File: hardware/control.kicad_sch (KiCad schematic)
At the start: 11 parts, among them J7 ESP32_DISP_P1, J8 ESP32_DISP_CN1, U1 MCP23017-E/SO, U2 TMP275AIDR

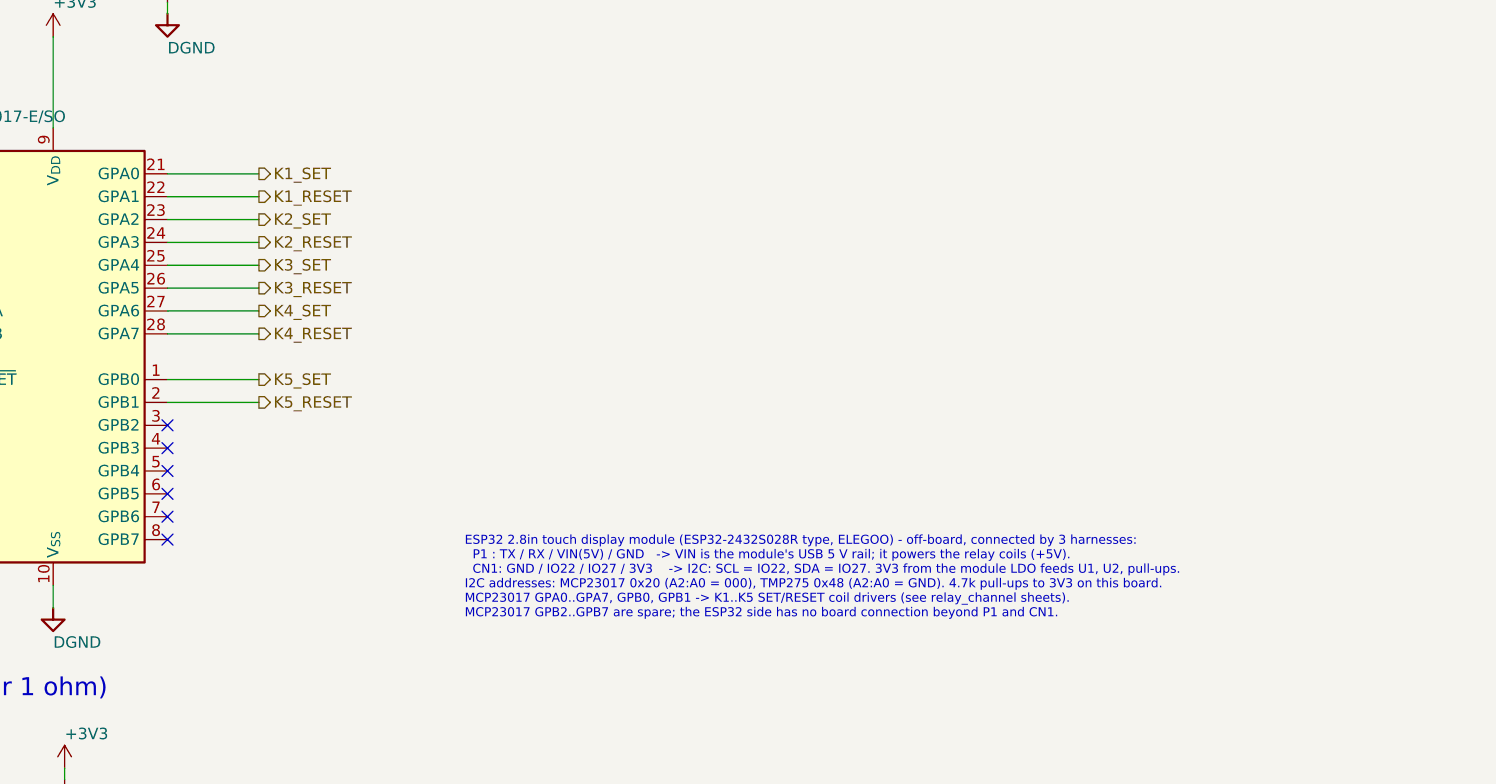
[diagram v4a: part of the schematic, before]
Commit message: Remap the MCP23017 GPIOs to the driver order: fan-out 30 vias -> 0
The coil lines were on GPA0..GPA7 (+ GPB0/1 for K5): the package row that
faces the board edge, in an order scrambled against the driver columns,
while GPB2..GPB7 - the row facing the drivers - sat unused. Every line had
to get off the wrong side of the chip and cross its neighbours.

  GPB0..GPB7  K4 S, K4 R, K1 S, K1 R, K2 S, K2 R, K3 S, K3 R  (columns' order)
  GPA0/GPA1   K5 RESET / K5 SET  (leave under the package to the right)
  GPA2..GPA7  spare

The firmware maps GPIO to coil by table; there is no firmware yet, so the
remap costs nothing there. Schematic change is in gen_schematics.py; only
control.kicad_sch changes, ERC clean, board nets synced from the netlist.

The whole control band is now hand-laid in route_hand.py: the fan-out, SDA/
SCL/3V3 under U1's body in pin order, ~RESET along the top edge, the harness
feeds between C3 and C4, +5V down the left edge, and straight B.Cu risers
from the TMP275 spine to the bus.

  MCP23017 coil lines   237 mm, 30 vias  ->  161 mm, 0 vias
  vias, whole board     101              ->  68

Also:
  route_pcb.py  vias now keep SEP from the other precision class. Two SRC_P
                vias sat 0.46 mm from RANGE_BUS; now 0 pairs under 0.5 mm.
  pcb_io.py     apply failed silently (never saved) on a board that already
                had tracks: GetNetsByName() breaks once tracks are removed.
                Look nets up with FindNet, and fail loudly if one is missing.

DRC: 0 errors, 0 unconnected, 0 schematic-parity issues, 56 benign
silk_over_copper. Silkscreen from the hand pass is untouched.

Co-Authored-By: Claude Opus 5 <noreply@anthropic.com>
Claude-Session: https://claude.ai/code/session_0128rWrsZDfCzkxQ1CZFxeXp
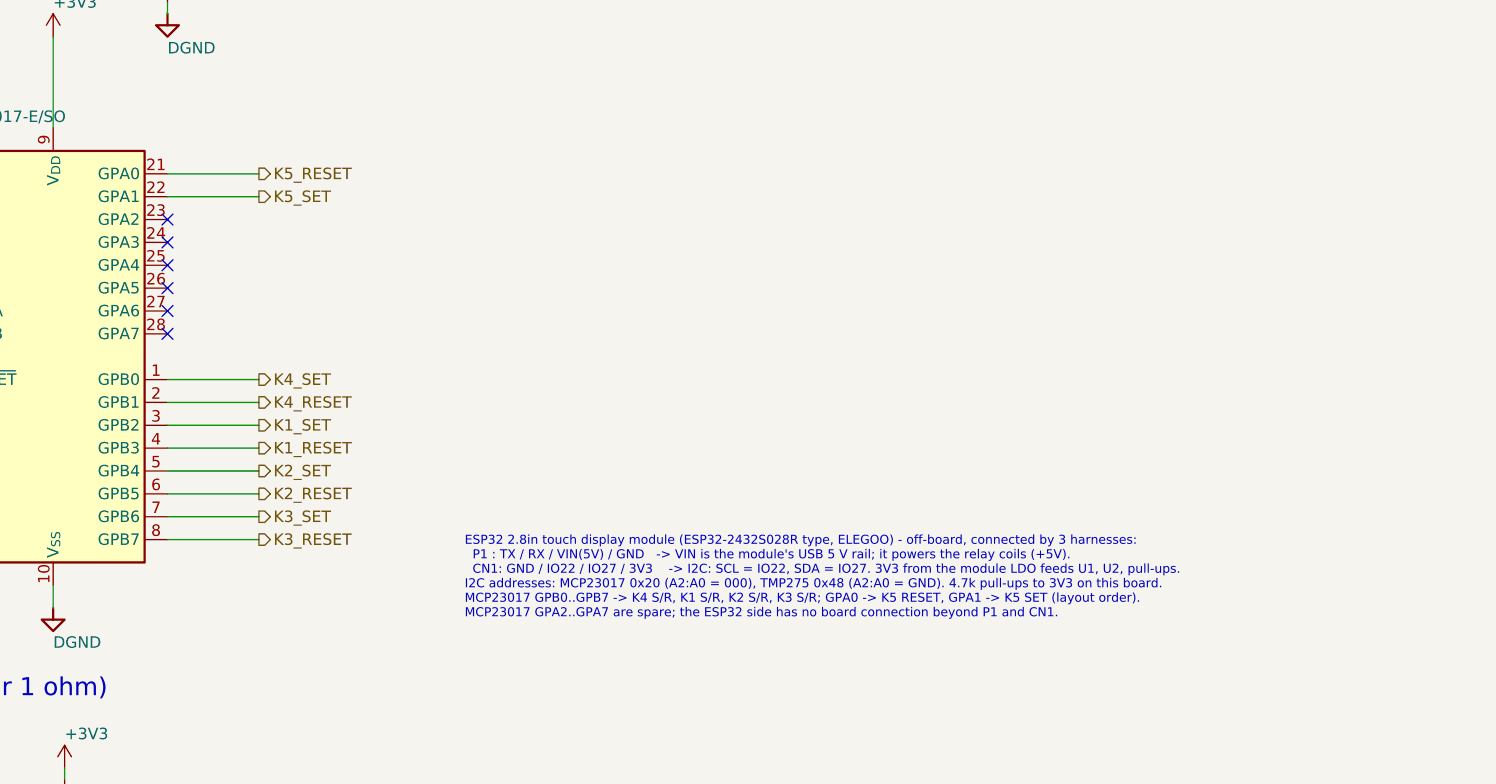
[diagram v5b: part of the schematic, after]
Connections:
- net K1_RESET: now also U1.4 (GPB3); no longer U1.22 (GPA1)
- net K1_SET: now also U1.3 (GPB2); no longer U1.21 (GPA0)
- net K2_RESET: now also U1.6 (GPB5); no longer U1.24 (GPA3)
- net K2_SET: now also U1.5 (GPB4); no longer U1.23 (GPA2)
- net K3_RESET: now also U1.8 (GPB7); no longer U1.26 (GPA5)
- net K3_SET: now also U1.7 (GPB6); no longer U1.25 (GPA4)
- net K4_RESET: now also U1.2 (GPB1); no longer U1.28 (GPA7)
- net K4_SET: now also U1.1 (GPB0); no longer U1.27 (GPA6)
- net K5_RESET: now also U1.21 (GPA0); no longer U1.2 (GPB1)
- net K5_SET: now also U1.22 (GPA1); no longer U1.1 (GPB0)
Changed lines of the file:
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@@
 	  ))
 	)
+	(wire (pts (xy 139.7 116.84) (xy 149.86 116.84)) (stroke (width 0) (type default)))
+	(hierarchical_label "K4_SET" (shape output) (at 149.86 116.84 0) (effects (font (size 1.27 1.27)) (justify left)))
+	(wire (pts (xy 139.7 119.38) (xy 149.86 119.38)) (stroke (width 0) (type default)))
+	(hierarchical_label "K4_RESET" (shape output) (at 149.86 119.38 0) (effects (font (size 1.27 1.27)) (justify left)))
+	(wire (pts (xy 139.7 121.92) (xy 149.86 121.92)) (stroke (width 0) (type default)))
+	(hierarchical_label "K1_SET" (shape output) (at 149.86 121.92 0) (effects (font (size 1.27 1.27)) (justify left)))
+	(wire (pts (xy 139.7 124.46) (xy 149.86 124.46)) (stroke (width 0) (type default)))
+	(hierarchical_label "K1_RESET" (shape output) (at 149.86 124.46 0) (effects (font (size 1.27 1.27)) (justify left)))
+	(wire (pts (xy 139.7 127) (xy 149.86 127)) (stroke (width 0) (type default)))
+	(hierarchical_label "K2_SET" (shape output) (at 149.86 127 0) (effects (font (size 1.27 1.27)) (justify left)))
+	(wire (pts (xy 139.7 129.54) (xy 149.86 129.54)) (stroke (width 0) (type default)))
+	(hierarchical_label "K2_RESET" (shape output) (at 149.86 129.54 0) (effects (font (size 1.27 1.27)) (justify left)))
+	(wire (pts (xy 139.7 132.08) (xy 149.86 132.08)) (stroke (width 0) (type default)))
+	(hierarchical_label "K3_SET" (shape output) (at 149.86 132.08 0) (effects (font (size 1.27 1.27)) (justify left)))
+	(wire (pts (xy 139.7 134.62) (xy 149.86 134.62)) (stroke (width 0) (type default)))
+	(hierarchical_label "K3_RESET" (shape output) (at 149.86 134.62 0) (effects (font (size 1.27 1.27)) (justify left)))
 	(wire (pts (xy 139.7 93.98) (xy 149.86 93.98)) (stroke (width 0) (type default)))
-	(hierarchical_label "K1_SET" (shape output) (at 149.86 93.98 0) (effects (font (size 1.27 1.27)) (justify left)))
+	(hierarchical_label "K5_RESET" (shape output) (at 149.86 93.98 0) (effects (font (size 1.27 1.27)) (justify left)))
 	(wire (pts (xy 139.7 96.52) (xy 149.86 96.52)) (stroke (width 0) (type default)))
-	(hierarchical_label "K1_RESET" (shape output) (at 149.86 96.52 0) (effects (font (size 1.27 1.27)) (justify left)))
-	(wire (pts (xy 139.7 99.06) (xy 149.86 99.06)) (stroke (width 0) (type default)))
-	(hierarchical_label "K2_SET" (shape output) (at 149.86 99.06 0) (effects (font (size 1.27 1.27)) (justify left)))
-	(wire (pts (xy 139.7 101.6) (xy 149.86 101.6)) (stroke (width 0) (type default)))
-	(hierarchical_label "K2_RESET" (shape output) (at 149.86 101.6 0) (effects (font (size 1.27 1.27)) (justify left)))
-	(wire (pts (xy 139.7 104.14) (xy 149.86 104.14)) (stroke (width 0) (type default)))
-	(hierarchical_label "K3_SET" (shape output) (at 149.86 104.14 0) (effects (font (size 1.27 1.27)) (justify left)))
-	(wire (pts (xy 139.7 106.68) (xy 149.86 106.68)) (stroke (width 0) (type default)))
-	(hierarchical_label "K3_RESET" (shape output) (at 149.86 106.68 0) (effects (font (size 1.27 1.27)) (justify left)))
-	(wire (pts (xy 139.7 109.22) (xy 149.86 109.22)) (stroke (width 0) (type default)))
-	(hierarchical_label "K4_SET" (shape output) (at 149.86 109.22 0) (effects (font (size 1.27 1.27)) (justify left)))
-	(wire (pts (xy 139.7 111.76) (xy 149.86 111.76)) (stroke (width 0) (type default)))
-	(hierarchical_label "K4_RESET" (shape output) (at 149.86 111.76 0) (effects (font (size 1.27 1.27)) (justify left)))
-	(wire (pts (xy 139.7 116.84) (xy 149.86 116.84)) (stroke (width 0) (type default)))
-	(hierarchical_label "K5_SET" (shape output) (at 149.86 116.84 0) (effects (font (size 1.27 1.27)) (justify left)))
-	(wire (pts (xy 139.7 119.38) (xy 149.86 119.38)) (stroke (width 0) (type default)))
-	(hierarchical_label "K5_RESET" (shape output) (at 149.86 119.38 0) (effects (font (size 1.27 1.27)) (justify left)))
-	(no_connect (at 139.7 121.92))
-	(no_connect (at 139.7 124.46))
-	(no_connect (at 139.7 127))
-	(no_connect (at 139.7 129.54))
-	(no_connect (at 139.7 132.08))
-	(no_connect (at 139.7 134.62))
+	(hierarchical_label "K5_SET" (shape output) (at 149.86 96.52 0) (effects (font (size 1.27 1.27)) (justify left)))
+	(no_connect (at 139.7 99.06))
+	(no_connect (at 139.7 101.6))
+	(no_connect (at 139.7 104.14))
+	(no_connect (at 139.7 106.68))
+	(no_connect (at 139.7 109.22))
+	(no_connect (at 139.7 111.76))
 	(symbol (lib_id "Device:C") (at 139.7 71.12 0) (unit 1) (body_style 1) (exclude_from_sim no) (in_bom yes) (on_board yes) (in_pos_files yes) (dnp no)
 	  (property "Reference" "C1" (at 142.24 69.85 0) (show_name no) (do_not_autoplace no) (effects (font (size 1.27 1.27)) (justify left)))
@@
 	  ))
 	)
-	(text "ESP32 2.8in touch display module (ESP32-2432S028R type, ELEGOO) - off-board, connected by 3 harnesses:\n  P1 : TX / RX / VIN(5V) / GND   -> VIN is the module's USB 5 V rail; it powers the relay coils (+5V).\n  CN1: GND / IO22 / IO27 / 3V3    -> I2C: SCL = IO22, SDA = IO27. 3V3 from the module LDO feeds U1, U2, pull-ups.\nI2C addresses: MCP23017 0x20 (A2:A0 = 000), TMP275 0x48 (A2:A0 = GND). 4.7k pull-ups to 3V3 on this board.\nMCP23017 GPA0..GPA7, GPB0, GPB1 -> K1..K5 SET/RESET coil drivers (see relay_channel sheets).\nMCP23017 GPB2..GPB7 are spare; the ESP32 side has no board connection beyond P1 and CN1." (at 172.72 143.51 0) (effects (font (size 1.0 1.0)) (justify left bottom)))
+	(text "ESP32 2.8in touch display module (ESP32-2432S028R type, ELEGOO) - off-board, connected by 3 harnesses:\n  P1 : TX / RX / VIN(5V) / GND   -> VIN is the module's USB 5 V rail; it powers the relay coils (+5V).\n  CN1: GND / IO22 / IO27 / 3V3    -> I2C: SCL = IO22, SDA = IO27. 3V3 from the module LDO feeds U1, U2, pull-ups.\nI2C addresses: MCP23017 0x20 (A2:A0 = 000), TMP275 0x48 (A2:A0 = GND). 4.7k pull-ups to 3V3 on this board.\nMCP23017 GPB0..GPB7 -> K4 S/R, K1 S/R, K2 S/R, K3 S/R; GPA0 -> K5 RESET, GPA1 -> K5 SET (layout order).\nMCP23017 GPA2..GPA7 are spare; the ESP32 side has no board connection beyond P1 and CN1." (at 172.72 143.51 0) (effects (font (size 1.0 1.0)) (justify left bottom)))
 	(text "ESP32 display module harness" (at 25.4 30.48 0) (effects (font (size 2.0 2.0)) (justify left bottom)))
 	(text "MCP23017 -> relay coil drivers" (at 66.04 80.01 0) (effects (font (size 2.0 2.0)) (justify left bottom)))
